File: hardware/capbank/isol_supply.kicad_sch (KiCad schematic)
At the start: 10 parts, among them U11 NXJ1S1212MC, U9 LM78L05ACZ

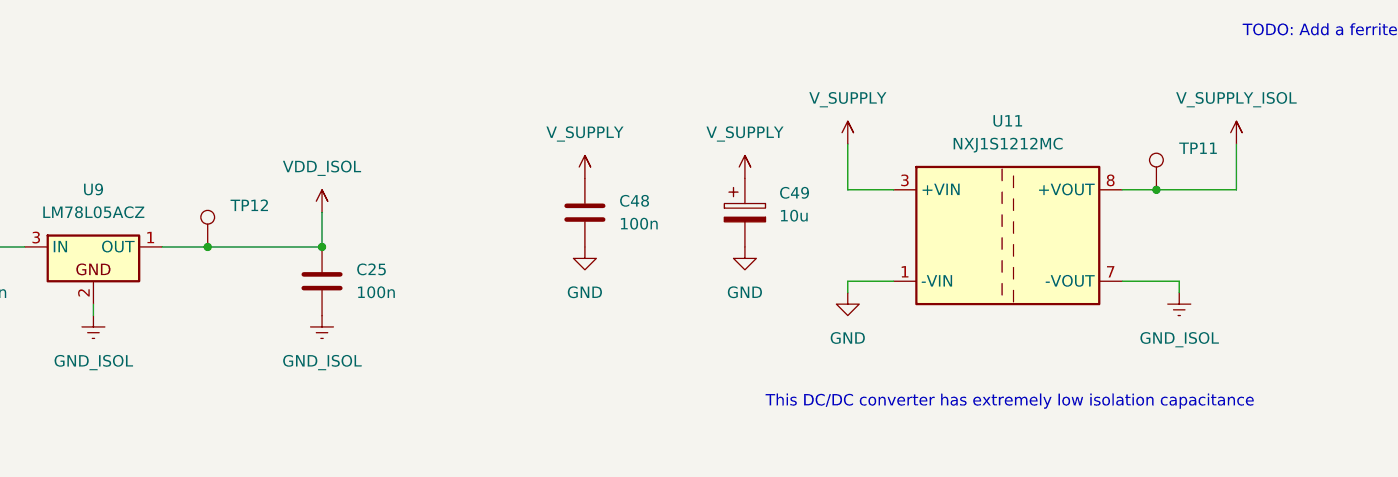
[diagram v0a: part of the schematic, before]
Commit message: Progress, layout nearly completed, build oscillator on breadboard
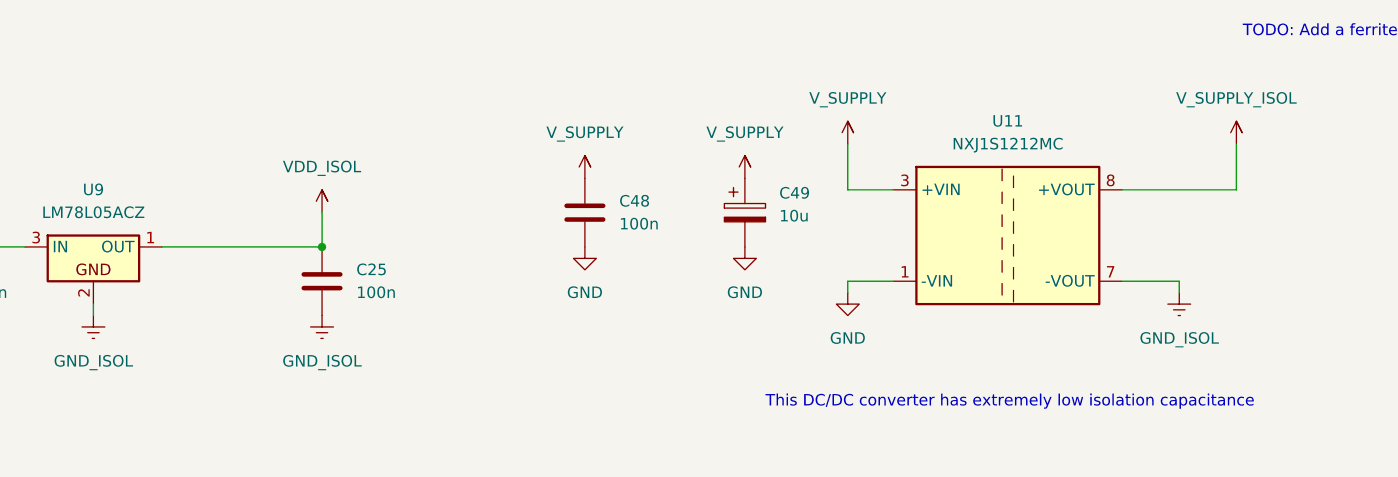
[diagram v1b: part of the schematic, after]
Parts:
- removed TP11, TP12: ~, TestPoint:TestPoint_THTPad_1.5x1.5mm_Drill0.7mm, symbol Connector:TestPoint
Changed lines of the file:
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@@
-	)
-	(junction
-		(at 177.8 88.9)
-		(diameter 0)
-		(color 0 0 0 0)
-	)
-	(junction
-		(at 72.39 95.25)
-		(diameter 0)
-		(color 0 0 0 0)
 	)
 	(junction
@@
 	(wire
 		(pts
-			(xy 173.99 88.9) (xy 177.8 88.9)
+			(xy 173.99 88.9) (xy 186.69 88.9)
 		)
 		(stroke
@@
 	(wire
 		(pts
-			(xy 67.31 95.25) (xy 72.39 95.25)
+			(xy 173.99 99.06) (xy 180.34 99.06)
 		)
 		(stroke
@@
 	(wire
 		(pts
-			(xy 177.8 88.9) (xy 186.69 88.9)
+			(xy 59.69 101.6) (xy 59.69 102.87)
 		)
 		(stroke
@@
 	(wire
 		(pts
-			(xy 173.99 99.06) (xy 180.34 99.06)
+			(xy 143.51 100.33) (xy 143.51 99.06)
 		)
 		(stroke
@@
 	(wire
 		(pts
-			(xy 59.69 101.6) (xy 59.69 102.87)
-		)
-		(stroke
-			(width 0)
-			(type default)
-		)
-	)
-	(wire
-		(pts
-			(xy 143.51 100.33) (xy 143.51 99.06)
-		)
-		(stroke
-			(width 0)
-			(type default)
-		)
-	)
-	(wire
-		(pts
-			(xy 72.39 95.25) (xy 85.09 95.25)
+			(xy 67.31 95.25) (xy 85.09 95.25)
 		)
 		(stroke
@@
 					(unit 1)
 				)
-			)
-		)
-	)
-	(symbol
-		(lib_id "Connector:TestPoint")
-		(at 177.8 88.9 0)
-		(unit 1)
-		(exclude_from_sim no)
-		(in_bom yes)
-		(on_board yes)
-		(dnp no)
-		(fields_autoplaced yes)
-		(property "Reference" "TP11"
-			(at 180.34 84.3279 0)
-			(effects
-				(font
-					(size 1.27 1.27)
-				)
-				(justify left)
-			)
-		)
-		(property "Value" "~"
-			(at 180.34 86.8679 0)
-			(effects
-				(font
-					(size 1.27 1.27)
-				)
-				(justify left)
-			)
-		)
-		(property "Footprint" "TestPoint:TestPoint_THTPad_1.5x1.5mm_Drill0.7mm"
-			(at 182.88 88.9 0)
-			(effects
-				(font
-					(size 1.27 1.27)
-				)
-				(hide yes)
-			)
-		)
-		(property "Datasheet" "~"
-			(at 182.88 88.9 0)
-			(effects
-				(font
-					(size 1.27 1.27)
-				)
-				(hide yes)
-			)
-		)
-		(property "Description" "test point"
-			(at 177.8 88.9 0)
-			(effects
-				(font
-					(size 1.27 1.27)
-				)
-				(hide yes)
-			)
-		)
-		(pin "1"
-		)
-		(instances
-			(project "capbank1"
-				(path "/461cb8a1-2d60-44a8-88b5-d61a3ba14a84/bb6379f6-afea-4713-b534-7575122a6ac9"
-					(reference "TP11")
-					(unit 1)
-				)
-			)
-		)
-	)
-	(symbol
-		(lib_id "Connector:TestPoint")
-		(at 72.39 95.25 0)
-		(unit 1)
-		(exclude_from_sim no)
-		(in_bom yes)
-		(on_board yes)
-		(dnp no)
-		(fields_autoplaced yes)
-		(property "Reference" "TP12"
-			(at 74.93 90.6779 0)
-			(effects
-				(font
-					(size 1.27 1.27)
-				)
-				(justify left)
-			)
-		)
-		(property "Value" "~"
-			(at 74.93 93.2179 0)
-			(effects
-				(font
-					(size 1.27 1.27)
-				)
-				(justify left)
-			)
-		)
-		(property "Footprint" "TestPoint:TestPoint_THTPad_1.5x1.5mm_Drill0.7mm"
-			(at 77.47 95.25 0)
-			(effects
-				(font
-					(size 1.27 1.27)
-				)
-				(hide yes)
-			)
-		)
-		(property "Datasheet" "~"
-			(at 77.47 95.25 0)
-			(effects
-				(font
-					(size 1.27 1.27)
-				)
-				(hide yes)
-			)
-		)
-		(property "Description" "test point"
-			(at 72.39 95.25 0)
-			(effects
-				(font
-					(size 1.27 1.27)
-				)
-				(hide yes)
-			)
-		)
-		(pin "1"
-		)
-		(instances
-			(project "capbank1"
-				(path "/461cb8a1-2d60-44a8-88b5-d61a3ba14a84/bb6379f6-afea-4713-b534-7575122a6ac9"
-					(reference "TP12")
-					(unit 1)
-				)
